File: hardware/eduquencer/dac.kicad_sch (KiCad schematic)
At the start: 14 parts

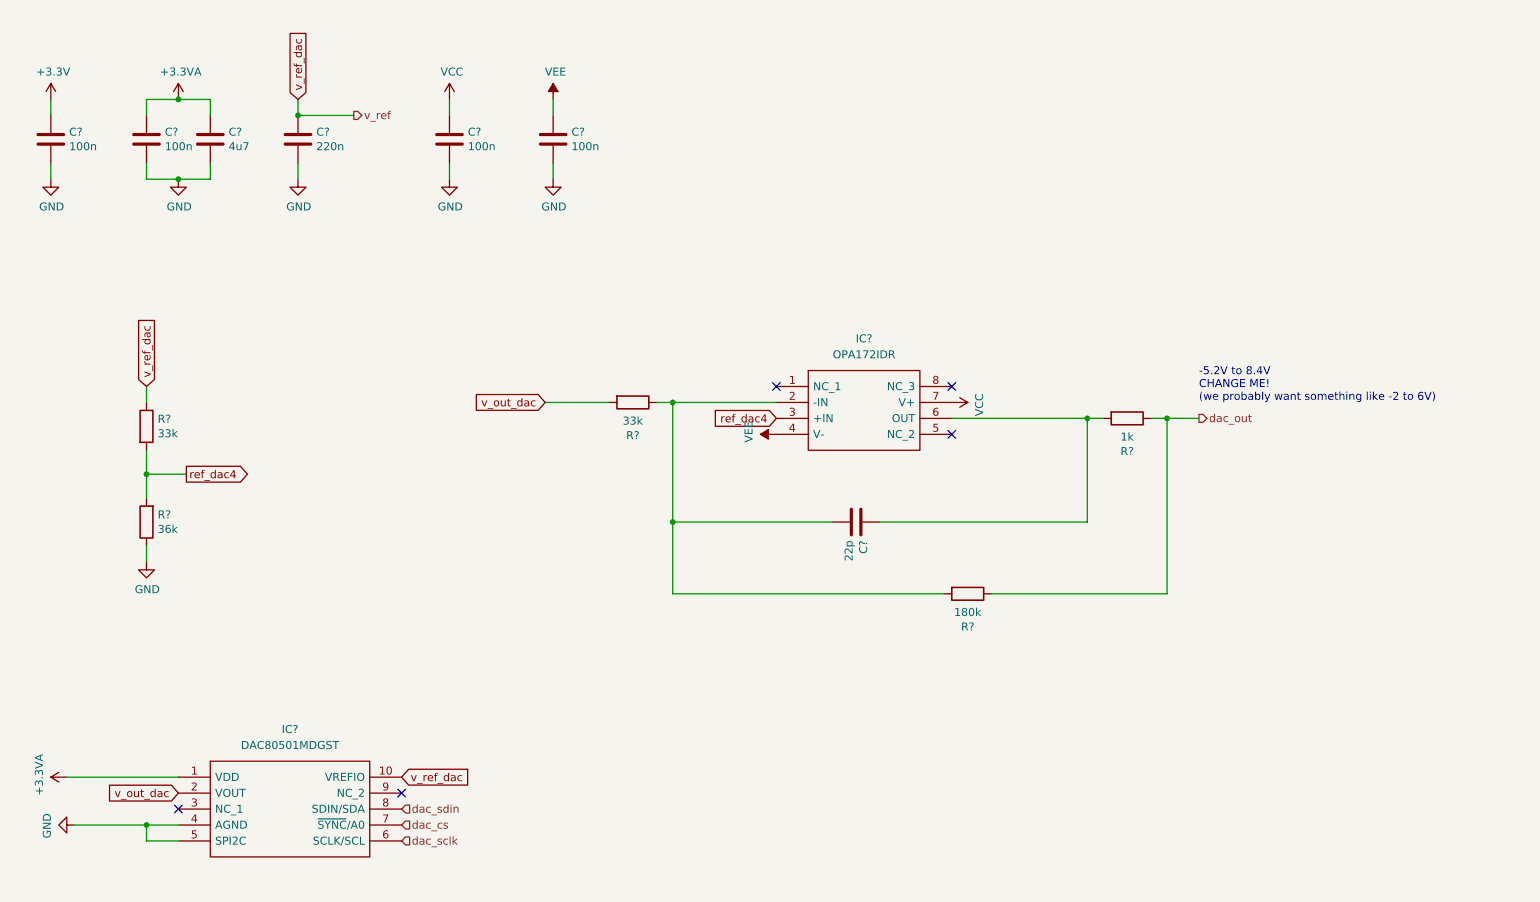
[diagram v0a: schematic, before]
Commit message: Hardware: add trigger in&outputs, wire rpi
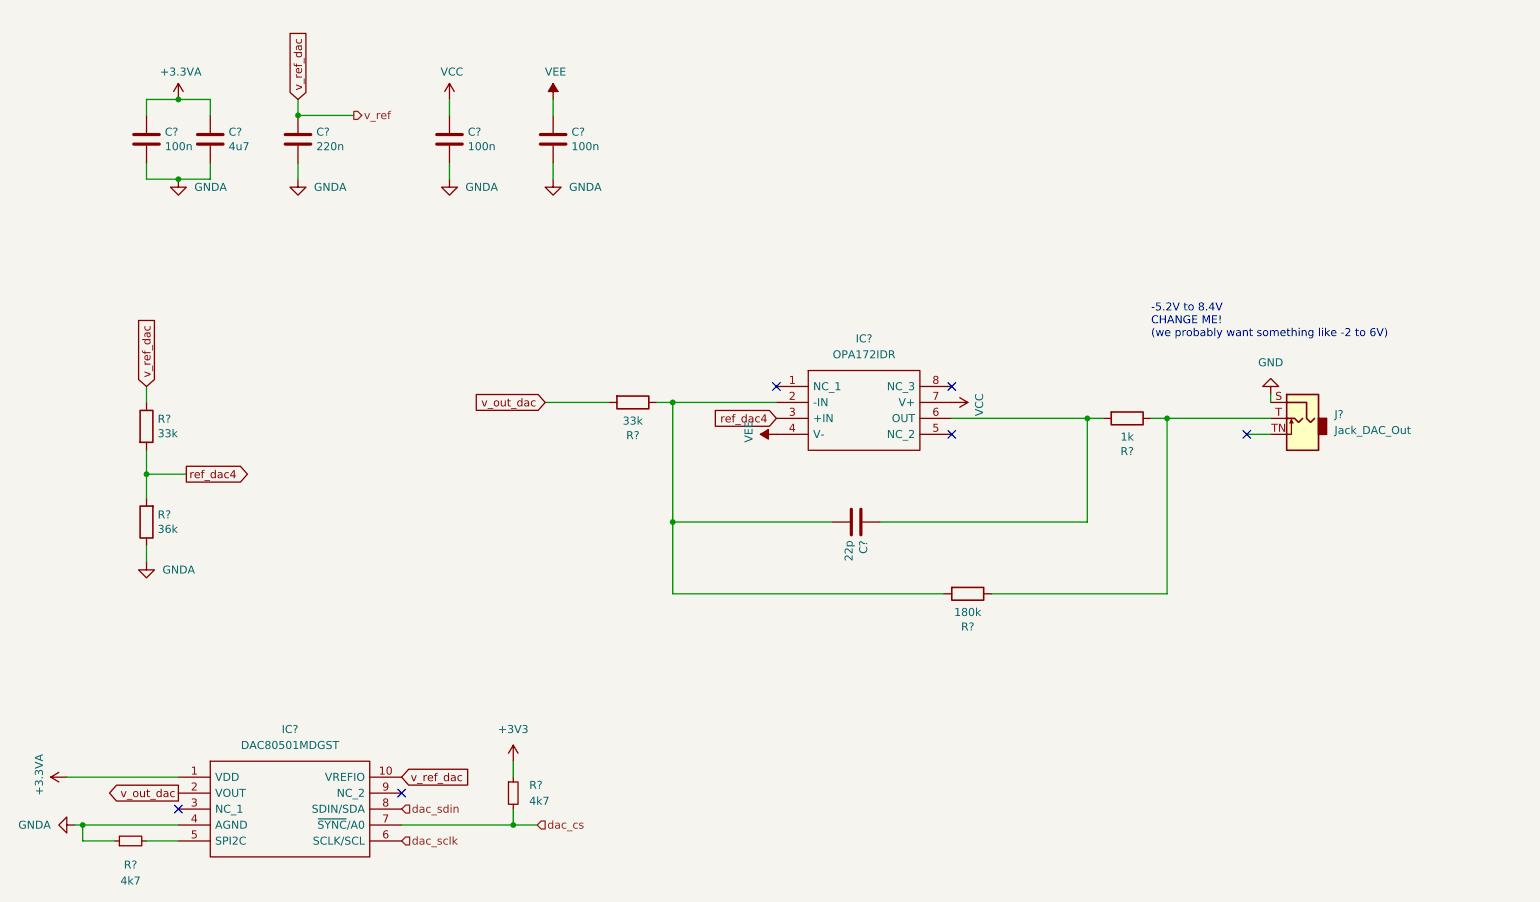
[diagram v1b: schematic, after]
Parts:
- removed C?: 100n, Capacitor_SMD:C_0603_1608Metric, symbol Device:C
- added J?: Jack_DAC_Out, AudioJacks:Jack_3.5mm_QingPu_WQP-PJ301BM_Vertical, symbol Connector:AudioJack2_SwitchT
- added R? (x2): 4k7, symbol Device:R_Small
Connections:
- net +3V3: now also R?.1
- net GND: now also J?.S; no longer C?.1, C?.1, C?.1, C?.1, C?.2, IC?.4 (AGND), IC?.5 (SPI2C), R?.1
- net dac_cs: now also R?.2
- net dac_out: no longer names the net of R?.1, R?.1
- net dac_out: now also J?.T
- new net: IC?.5 (SPI2C), R?.2
- new net GNDA: C?.1, C?.1, C?.1, C?.1, C?.2, IC?.4 (AGND), R?.1, R?.1
- no-connect marks 5 -> 6

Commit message: Hardware: add test points, tiny cleanup
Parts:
- C? (x3): LCSC C14663 -> (none); LCSC Part # C14663 -> (none)
- C?: LCSC C19666 -> (none); LCSC Part # C19666 -> (none)
- C?: LCSC C21120 -> (none); LCSC Part # C21120 -> (none)
- C?: LCSC C1653 -> (none); LCSC Part # C1653 -> (none)
- J?: value Jack_DAC_Out -> Out A
- R?: LCSC C23147 -> (none); LCSC Part # C23147 -> (none)
- R? (x2): LCSC C4216 -> (none); LCSC Part # C4216 -> (none)
- R?: LCSC C21190 -> (none); LCSC Part # C21190 -> (none)
- R?: LCSC C22827 -> (none); LCSC Part # C22827 -> (none)
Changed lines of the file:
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@@
   (symbol (lib_id "power:+3.3VA") (at 57.15 34.29 0) (unit 1)
     (in_bom yes) (on_board yes)
-    (property "Reference" "#PWR?" (id 0) (at 57.15 38.1 0)
+    (property "Reference" "#PWR0229" (id 0) (at 57.15 38.1 0)
       (effects (font (size 1.27 1.27)) hide)
     )
@@
       (effects (font (size 1.27 1.27)) hide)
     )
-    (property "LCSC Part #" "C14663" (id 4) (at 52.07 40.64 0)
-      (effects (font (size 1.27 1.27)) hide)
-    )
-    (property "LCSC" "C14663" (id 5) (at 52.07 40.64 0)
-      (effects (font (size 1.27 1.27)) hide)
-    )
     (pin "1")
     (pin "2")
@@
       (effects (font (size 1.27 1.27)) hide)
     )
-    (property "LCSC Part #" "C19666" (id 4) (at 62.23 40.64 0)
-      (effects (font (size 1.27 1.27)) hide)
-    )
-    (property "LCSC" "C19666" (id 5) (at 62.23 40.64 0)
-      (effects (font (size 1.27 1.27)) hide)
-    )
     (pin "1")
     (pin "2")
@@
       (effects (font (size 1.27 1.27)) hide)
     )
-    (property "LCSC Part #" "C21120" (id 4) (at 76.2 40.64 0)
-      (effects (font (size 1.27 1.27)) hide)
-    )
-    (property "LCSC" "C21120" (id 5) (at 76.2 40.64 0)
-      (effects (font (size 1.27 1.27)) hide)
-    )
     (pin "1")
     (pin "2")
@@
     )
     (property "Datasheet" "~" (id 3) (at 52.07 101.6 0)
-      (effects (font (size 1.27 1.27)) hide)
-    )
-    (property "LCSC Part #" "C23147" (id 4) (at 52.07 101.6 0)
-      (effects (font (size 1.27 1.27)) hide)
-    )
-    (property "LCSC" "C23147" (id 5) (at 52.07 101.6 0)
       (effects (font (size 1.27 1.27)) hide)
     )
@@
       (effects (font (size 1.27 1.27)) hide)
     )
-    (property "LCSC Part #" "C4216" (id 4) (at 129.54 82.55 0)
-      (effects (font (size 1.27 1.27)) hide)
-    )
-    (property "LCSC" "C4216" (id 5) (at 129.54 82.55 0)
-      (effects (font (size 1.27 1.27)) hide)
-    )
     (pin "1")
     (pin "2")
@@
     )
     (property "Datasheet" "~" (id 3) (at 52.07 86.36 0)
-      (effects (font (size 1.27 1.27)) hide)
-    )
-    (property "LCSC Part #" "C4216" (id 4) (at 52.07 86.36 0)
-      (effects (font (size 1.27 1.27)) hide)
-    )
-    (property "LCSC" "C4216" (id 5) (at 52.07 86.36 0)
       (effects (font (size 1.27 1.27)) hide)
     )
@@
       (effects (font (size 1.27 1.27)) hide)
     )
-    (property "LCSC Part #" "C21190" (id 4) (at 208.28 85.09 0)
-      (effects (font (size 1.27 1.27)) hide)
-    )
-    (property "LCSC" "C21190" (id 5) (at 208.28 85.09 0)
-      (effects (font (size 1.27 1.27)) hide)
-    )
     (pin "1")
     (pin "2")
@@
       (effects (font (size 1.27 1.27)) hide)
     )
-    (property "LCSC Part #" "C22827" (id 4) (at 182.88 113.03 0)
-      (effects (font (size 1.27 1.27)) hide)
-    )
-    (property "LCSC" "C22827" (id 5) (at 182.88 113.03 0)
-      (effects (font (size 1.27 1.27)) hide)
-    )
     (pin "1")
     (pin "2")
@@
       (effects (font (size 1.27 1.27)) hide)
     )
-    (property "LCSC Part #" "C14663" (id 4) (at 100.33 40.64 0)
-      (effects (font (size 1.27 1.27)) hide)
-    )
-    (property "LCSC" "C14663" (id 5) (at 100.33 40.64 0)
-      (effects (font (size 1.27 1.27)) hide)
-    )
     (pin "1")
     (pin "2")
@@
       (effects (font (size 1.27 1.27)) hide)
     )
-    (property "LCSC Part #" "C14663" (id 4) (at 116.84 40.64 0)
-      (effects (font (size 1.27 1.27)) hide)
-    )
-    (property "LCSC" "C14663" (id 5) (at 116.84 40.64 0)
-      (effects (font (size 1.27 1.27)) hide)
-    )
     (pin "1")
     (pin "2")
@@
       (effects (font (size 1.27 1.27)) hide)
     )
-    (property "LCSC Part #" "C1653" (id 4) (at 165.1 101.6 0)
-      (effects (font (size 1.27 1.27)) hide)
-    )
-    (property "LCSC" "C1653" (id 5) (at 165.1 101.6 0)
-      (effects (font (size 1.27 1.27)) hide)
-    )
     (pin "1")
     (pin "2")
@@
   (symbol (lib_id "power:VCC") (at 100.33 34.29 0) (unit 1)
     (in_bom yes) (on_board yes)
-    (property "Reference" "#PWR?" (id 0) (at 100.33 38.1 0)
+    (property "Reference" "#PWR0230" (id 0) (at 100.33 38.1 0)
       (effects (font (size 1.27 1.27)) hide)
     )
@@
   (symbol (lib_id "power:VEE") (at 116.84 34.29 0) (unit 1)
     (in_bom yes) (on_board yes)
-    (property "Reference" "#PWR?" (id 0) (at 116.84 38.1 0)
+    (property "Reference" "#PWR0234" (id 0) (at 116.84 38.1 0)
       (effects (font (size 1.27 1.27)) hide)
     )
@@
   (symbol (lib_id "power:VEE") (at 152.4 87.63 90) (unit 1)
     (in_bom yes) (on_board yes)
-    (property "Reference" "#PWR?" (id 0) (at 156.21 87.63 0)
+    (property "Reference" "#PWR0227" (id 0) (at 156.21 87.63 0)
       (effects (font (size 1.27 1.27)) hide)
     )
@@
   (symbol (lib_id "power:+3V3") (at 110.49 139.7 0) (unit 1)
     (in_bom yes) (on_board yes) (fields_autoplaced)
-    (property "Reference" "#PWR?" (id 0) (at 110.49 143.51 0)
+    (property "Reference" "#PWR0224" (id 0) (at 110.49 143.51 0)
       (effects (font (size 1.27 1.27)) hide)
     )
@@
   (symbol (lib_id "power:VCC") (at 180.34 82.55 270) (unit 1)
     (in_bom yes) (on_board yes)
-    (property "Reference" "#PWR?" (id 0) (at 176.53 82.55 0)
+    (property "Reference" "#PWR0226" (id 0) (at 176.53 82.55 0)
       (effects (font (size 1.27 1.27)) hide)
     )
@@
       (effects (font (size 1.27 1.27)) (justify right))
     )
-    (property "Value" "Jack_DAC_Out" (id 1) (at 241.3 86.9949 0)
+    (property "Value" "Out A" (id 1) (at 241.3 86.9949 0)
       (effects (font (size 1.27 1.27)) (justify right))
     )
@@
   (symbol (lib_id "power:GNDA") (at 76.2 46.99 0) (unit 1)
     (in_bom yes) (on_board yes) (fields_autoplaced)
-    (property "Reference" "#PWR?" (id 0) (at 76.2 53.34 0)
+    (property "Reference" "#PWR0231" (id 0) (at 76.2 53.34 0)
       (effects (font (size 1.27 1.27)) hide)
     )
@@
   (symbol (lib_id "power:GNDA") (at 100.33 46.99 0) (unit 1)
     (in_bom yes) (on_board yes) (fields_autoplaced)
-    (property "Reference" "#PWR?" (id 0) (at 100.33 53.34 0)
+    (property "Reference" "#PWR0232" (id 0) (at 100.33 53.34 0)
       (effects (font (size 1.27 1.27)) hide)
     )
@@
   (symbol (lib_id "power:GNDA") (at 40.64 149.86 270) (unit 1)
     (in_bom yes) (on_board yes) (fields_autoplaced)
-    (property "Reference" "#PWR?" (id 0) (at 34.29 149.86 0)
+    (property "Reference" "#PWR0221" (id 0) (at 34.29 149.86 0)
       (effects (font (size 1.27 1.27)) hide)
     )
@@
   (symbol (lib_id "power:GNDA") (at 57.15 46.99 0) (unit 1)
     (in_bom yes) (on_board yes) (fields_autoplaced)
-    (property "Reference" "#PWR?" (id 0) (at 57.15 53.34 0)
+    (property "Reference" "#PWR0228" (id 0) (at 57.15 53.34 0)
       (effects (font (size 1.27 1.27)) hide)
     )
@@
   (symbol (lib_id "power:GND") (at 231.14 81.28 180) (unit 1)
     (in_bom yes) (on_board yes) (fields_autoplaced)
-    (property "Reference" "#PWR?" (id 0) (at 231.14 74.93 0)
+    (property "Reference" "#PWR0225" (id 0) (at 231.14 74.93 0)
       (effects (font (size 1.27 1.27)) hide)
     )
@@
   (symbol (lib_id "power:GNDA") (at 116.84 46.99 0) (unit 1)
     (in_bom yes) (on_board yes) (fields_autoplaced)
-    (property "Reference" "#PWR?" (id 0) (at 116.84 53.34 0)
+    (property "Reference" "#PWR0233" (id 0) (at 116.84 53.34 0)
       (effects (font (size 1.27 1.27)) hide)
     )
@@
   (symbol (lib_id "power:+3.3VA") (at 39.37 142.24 90) (unit 1)
     (in_bom yes) (on_board yes)
-    (property "Reference" "#PWR?" (id 0) (at 43.18 142.24 0)
+    (property "Reference" "#PWR0222" (id 0) (at 43.18 142.24 0)
       (effects (font (size 1.27 1.27)) hide)
     )
@@
   (symbol (lib_id "power:GNDA") (at 52.07 107.95 0) (unit 1)
     (in_bom yes) (on_board yes) (fields_autoplaced)
-    (property "Reference" "#PWR?" (id 0) (at 52.07 114.3 0)
-      (effects (font (size 1.27 1.27)) hide)
-    )
+    (property "Reference" "#PWR0223" (id 0) (at 52.07 114.3 0)
+      (effects (font (size 1.27 1.27)) hide)
+    )

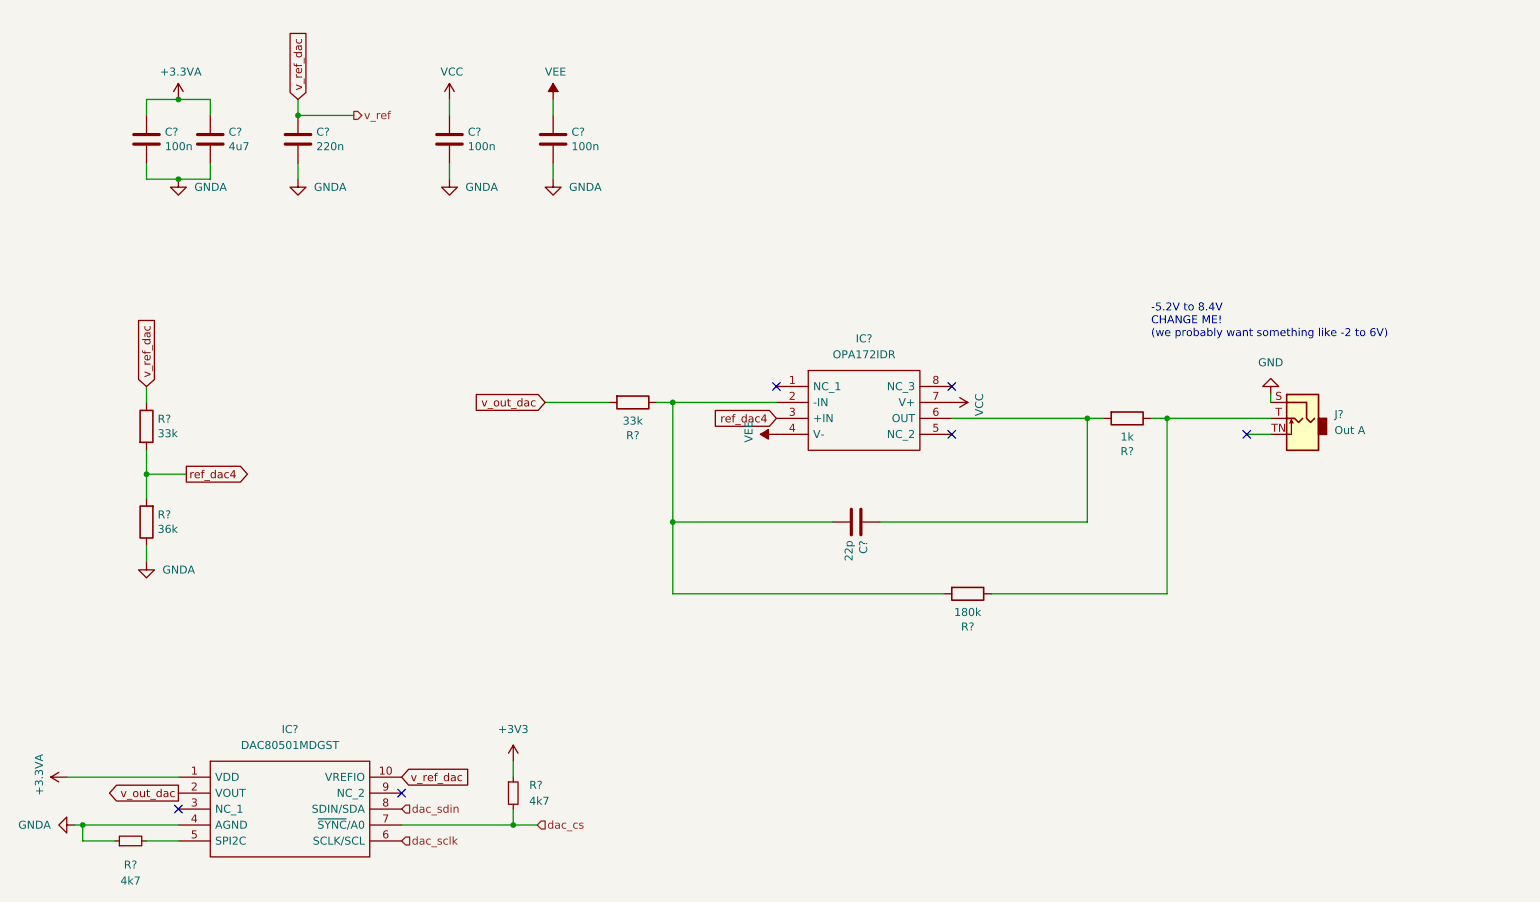
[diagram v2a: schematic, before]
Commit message: Hardware: update models, annotate, fix ERC issues
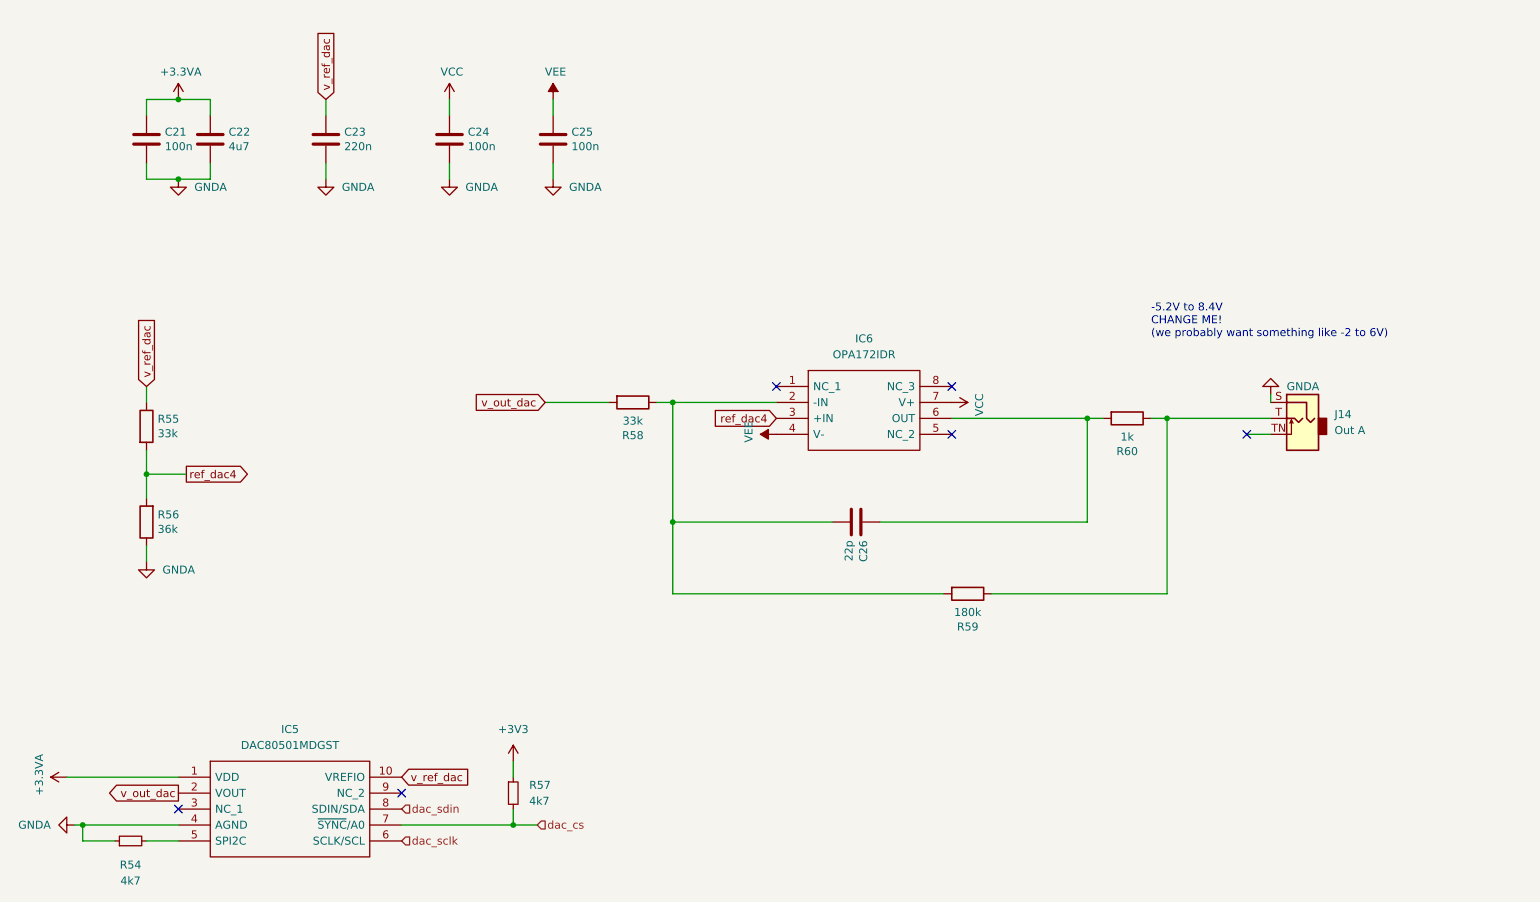
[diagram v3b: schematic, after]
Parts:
- gave numbers to parts that had none: 16
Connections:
- net GND is gone; now on net GNDA: J14.S
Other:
- moved on the sheet: C23
